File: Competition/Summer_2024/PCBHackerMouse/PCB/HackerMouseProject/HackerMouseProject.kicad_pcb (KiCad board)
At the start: 2 copper layers, 38 parts, among them J1 MicroUSB, SW1 1825910-6, SW3 1825910-6, U1 ESP32-S3R8, U2 W25Q128JVSIM_TR, Y1 ECS-400-10-37B2-CKY-TR

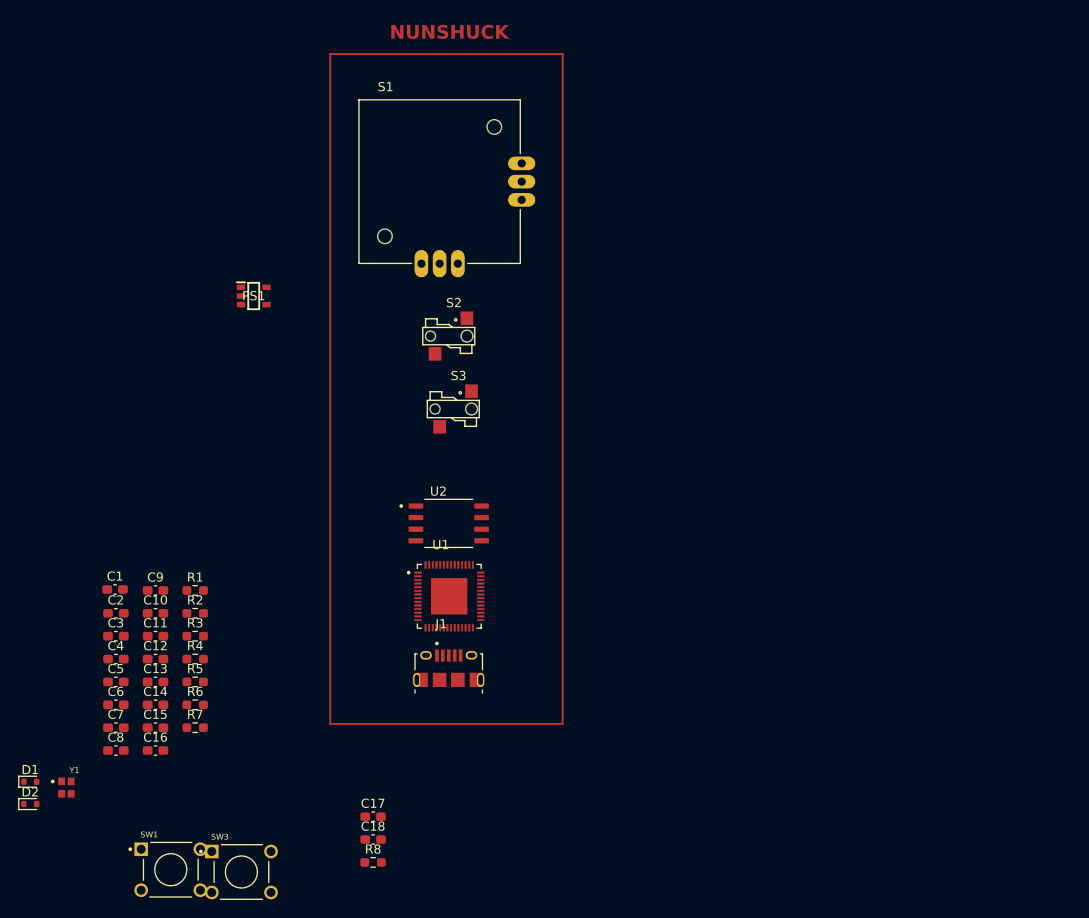
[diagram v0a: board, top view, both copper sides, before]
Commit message: First placement of component
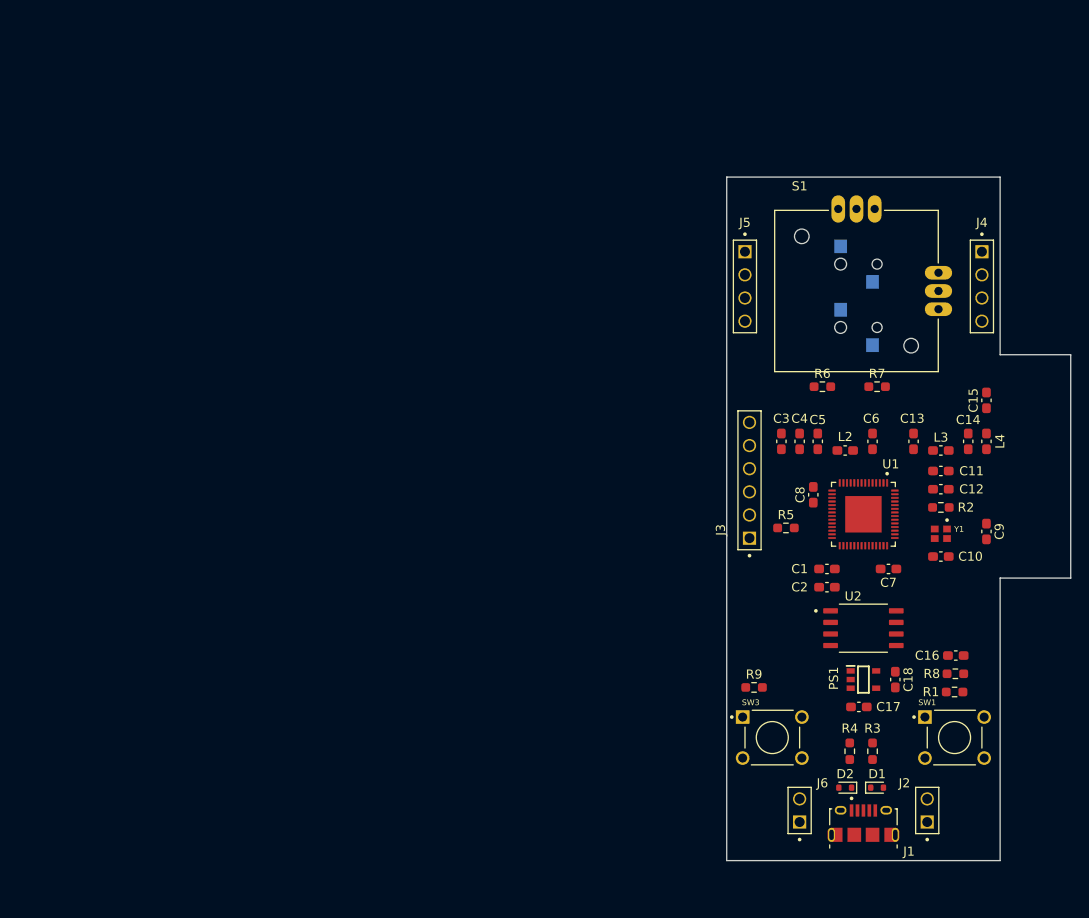
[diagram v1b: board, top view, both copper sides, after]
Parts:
- added J2: UART, Header2:WURTH_61300211121, F.Cu at (182.0, 103.5)
- added J3: Micro_SD, Header6:WURTH_61300611121, F.Cu at (162.5, 67.3)
- added J4: Header4, Header4:WURTH_61300411121, F.Cu at (188.0, 46.0)
- added J5: Header4, Header4:WURTH_61300411121, F.Cu at (162.0, 46.0)
- added J6: POWER, Header2:WURTH_61300211121, F.Cu at (168.0, 103.5)
- added L2: 2.4nH, Capacitor_SMD:C_0603_1608Metric_Pad1.08x0.95mm_HandSolder, F.Cu at (173.0, 64.0)
- added L3: 2.4 nH, Capacitor_SMD:C_0603_1608Metric_Pad1.08x0.95mm_HandSolder, F.Cu at (183.5, 64.0)
- added L4: L, Capacitor_SMD:C_0603_1608Metric_Pad1.08x0.95mm_HandSolder, F.Cu at (188.5, 63.0)
- added R9: 10k, Resistor_SMD:R_0603_1608Metric_Pad0.98x0.95mm_HandSolder, F.Cu at (163.0, 90.0)
- C10, C9: value C -> 12pF
- C13, C14: value C -> 1pF
- R2: value R -> 22
- S2, S3: moved to B.Cu
- moved Y1 99.9 mm to (183.5, 73.1), turned to -90 degrees
- moved C15 98.0 mm to (188.5, 58.5), turned to 90 degrees
- moved C14 93.7 mm to (186.5, 63.0), turned to 90 degrees
- moved D1 92.9 mm to (176.5, 101.0)
- moved C9 91.4 mm to (188.5, 72.9), turned to -90 degrees
- moved D2 89.4 mm to (173.0, 101.0), turned to 180 degrees
- moved C16 88.4 mm to (185.1, 86.5), turned to 180 degrees
- moved C12 88.2 mm to (183.5, 68.2)
- moved C11 88.1 mm to (183.5, 66.2)
- moved C6 87.9 mm to (176.0, 63.0), turned to 90 degrees
- moved C13 87.3 mm to (180.5, 63.0), turned to 90 degrees
- moved SW1 87.2 mm to (185.0, 95.5)
- moved C7 86.5 mm to (177.8, 77.0), turned to 180 degrees
- moved C10 86.4 mm to (183.5, 75.6)
- moved R1 84.1 mm to (185.0, 90.5)
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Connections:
- D2 pad 1: /ESP_D- -> Net-(D2-K)
- J1 pad 2: Net-(J1-D-) -> Net-(D2-K)
- R4 pad 2: Net-(J1-D-) -> Net-(D2-K)
- U1 pad 16: unconnected-(U1-GPIO11-Pad16) -> /MOSI
- U1 pad 17: unconnected-(U1-GPIO12-Pad17) -> /SCK
- U1 pad 18: unconnected-(U1-GPIO13-Pad18) -> /MISO
- U1 pad 19: unconnected-(U1-GPIO14-Pad19) -> /CS1
- U1 pad 27: unconnected-(U1-GPIO21-Pad27) -> /GPIO21
- U1 pad 38: unconnected-(U1-GPIO33-Pad38) -> /GPIO33
- U1 pad 39: unconnected-(U1-GPIO34-Pad39) -> /GPIO34
- U1 pad 40: unconnected-(U1-GPIO35-Pad40) -> /GPIO35
- U1 pad 41: unconnected-(U1-GPIO36-Pad41) -> /GPIO36
- U1 pad 42: unconnected-(U1-GPIO37-Pad42) -> /GPIO37
- U1 pad 43: unconnected-(U1-GPIO38-Pad43) -> /GPIO38
- U1 pad 49: unconnected-(U1-U0TXD-Pad49) -> /ESP_TX
- U1 pad 50: unconnected-(U1-U0RXD-Pad50) -> /ESP_RX
- U1 pad 51: unconnected-(U1-GPIO45-Pad51) -> /GPIO45
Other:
- board outline added: 37.8 x 75 mm
- copper layers 2 -> 4
- board text removed: "NUNSHUCK"

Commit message: Start Tracing PCB
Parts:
- added R10: 10k, Resistor_SMD:R_0603_1608Metric_Pad0.98x0.95mm_HandSolder, F.Cu at (170.4, 90.0)
- moved S3 11.6 mm to (176.0, 39.0)
- moved S2 8.14 mm to (167.8, 39.0)
- moved C17 5.81 mm to (170.4, 88.0), turned to 180 degrees
- moved C8 3.80 mm to (165.8, 69.5)
- moved C10 2.86 mm to (181.0, 74.2), turned to -90 degrees
- moved S1 2.38 mm to (175.0, 44.2), turned to 0 degrees
- moved C9 1.50 mm to (187.0, 72.9)
- moved R5 1.35 mm to (166.0, 73.8)
- moved Y1 0.46 mm to (183.8, 72.8)
- moved C11 0.25 mm to (183.5, 66.0)
- moved C12 0.25 mm to (183.5, 68.0)
- moved R1 0.10 mm to (185.1, 90.5)
- turned R3 to -90 degrees
- turned R4 to -90 degrees
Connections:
- PS1 pad 3: +5V -> Net-(PS1-STBY)
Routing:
- net +5V: track 0.00 -> 83.4 mm
- net +3V3: track 0.00 -> 79.3 mm, vias 0 -> 2
- net /BOOT: track 0.00 -> 51.0 mm, vias 0 -> 2
- net /ESP_D+: track 0.00 -> 33.7 mm
- net /ESP_D-: track 0.00 -> 33.3 mm
- net /RESET: track 0.00 -> 25.7 mm, vias 0 -> 2
- net /SPIWP: track 0.00 -> 23.1 mm
- net /SPID: track 0.00 -> 17.7 mm
- net /SPICLK: track 0.00 -> 16.3 mm
- net /SPIHD: track 0.00 -> 14.6 mm
- net /SPIQ: track 0.00 -> 12.9 mm, vias 0 -> 2
- net VDD_SPI: track 0.00 -> 12.6 mm
- net /CS1: track 0.00 -> 12.0 mm, vias 0 -> 1
- net /SCK: track 0.00 -> 11.8 mm
- net /MISO: track 0.00 -> 10.5 mm, vias 0 -> 1
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
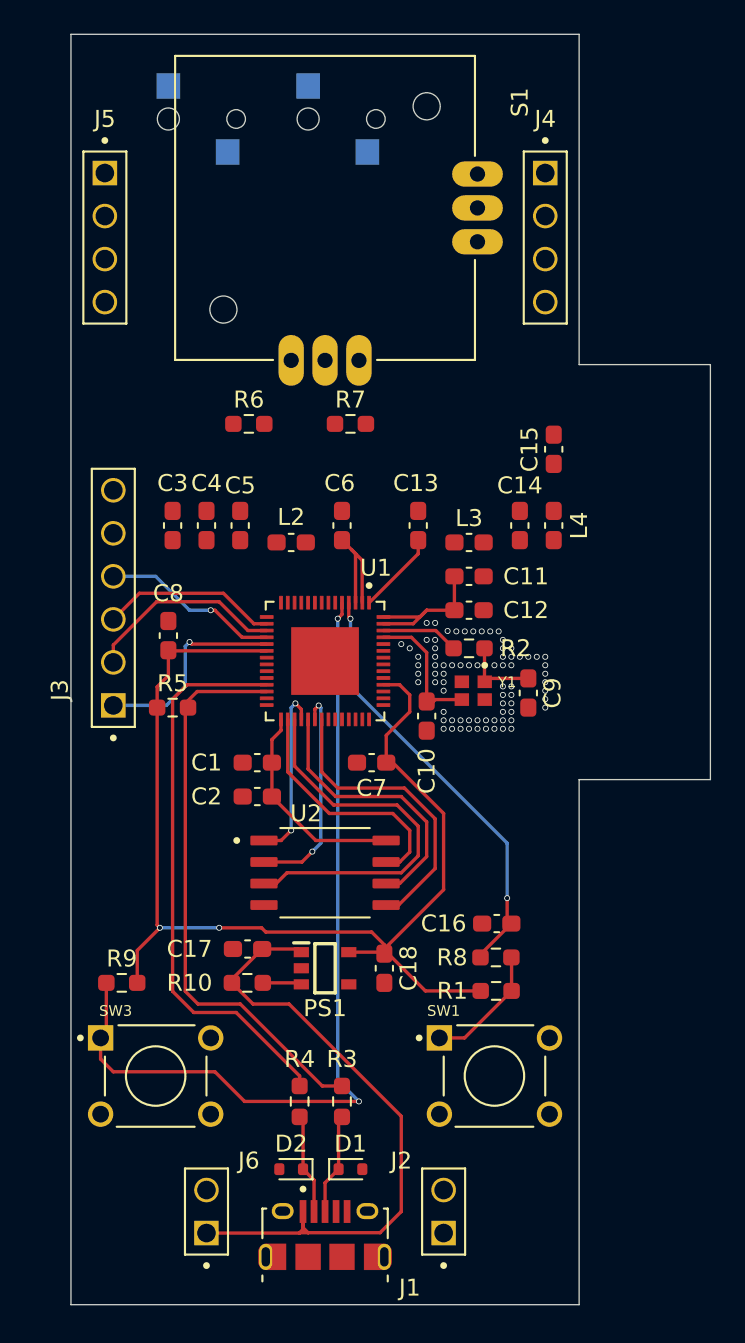
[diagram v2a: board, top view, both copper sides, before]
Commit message: PCB without antenna
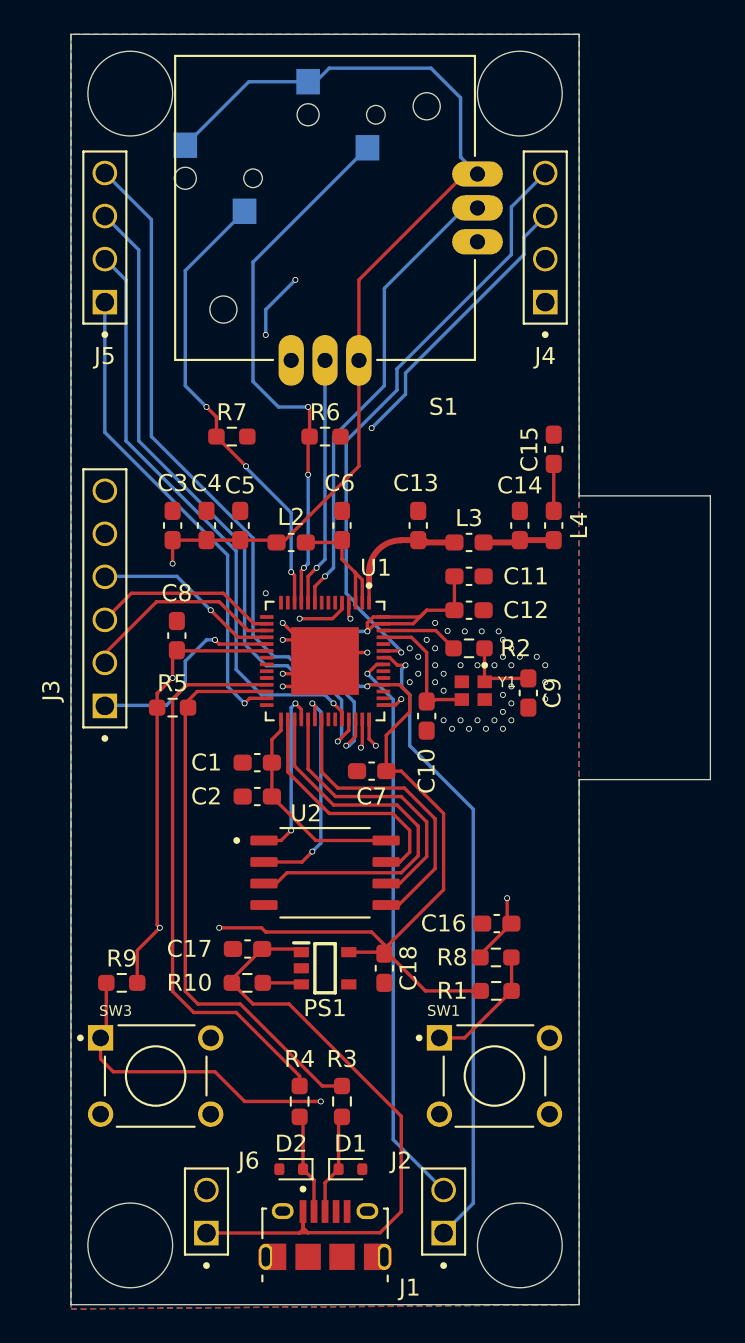
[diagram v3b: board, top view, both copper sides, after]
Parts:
- moved S2 8.25 mm to (176.0, 38.8)
- moved S3 8.05 mm to (168.8, 42.5)
- moved R7 7.04 mm to (169.5, 57.8)
- moved R6 4.56 mm to (175.0, 57.8)
- moved J3 0.50 mm to (162.0, 67.3)
- moved C7 0.50 mm to (177.8, 77.5)
- moved C8 0.50 mm to (166.2, 69.5)
- turned J4 to 90 degrees
- turned J5 to 90 degrees
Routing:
- net +3V3: track 79.3 -> 154.0 mm, vias 2 -> 6
- net /GPIO37: track 0.00 -> 47.9 mm, vias 0 -> 3
- net /GPIO36: track 0.00 -> 46.7 mm, vias 0 -> 1
- net /GPIO35: track 0.00 -> 43.2 mm, vias 0 -> 1
- net /GPIO34: track 0.00 -> 39.9 mm, vias 0 -> 1
- net /ESP_RX: track 0.00 -> 37.6 mm, vias 0 -> 1
- net /GPIO38: track 0.00 -> 36.1 mm, vias 0 -> 2
- net /GPIO45: track 0.00 -> 35.6 mm, vias 0 -> 1
- net /GPIO33: track 0.00 -> 35.2 mm, vias 0 -> 1
- net /ESP_TX: track 0.00 -> 33.5 mm, vias 0 -> 1
- net /BUT_1: track 0.00 -> 32.3 mm, vias 0 -> 3
- net /GPIO21: track 0.00 -> 28.5 mm, vias 0 -> 1
- net /JOY_X: track 0.00 -> 27.7 mm, vias 0 -> 1
- net /BUT_2: track 0.00 -> 27.2 mm, vias 0 -> 3
- net GND: track 0.00 -> 15.1 mm, vias 75 -> 46
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- added copper zone on B.Cu, net GND
- added copper zone on F.Cu, net GND
- added copper zone on In1.Cu, net GND
- added copper zone on In2.Cu, net GND
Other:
- outline, holes or cut-outs redrawn
